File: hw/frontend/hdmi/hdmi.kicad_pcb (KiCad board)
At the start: 6 copper layers, 100 x 100 mm, 208 parts, among them J801 SAMTEC_QSH-090-D, P201 HDMI, P301 HDMI, P302 CONN_02X05, P601 CONN_02X03, P602 CONN_02X05, P801 CONN_01X02, U202 TPD12S520, U301 TPD12S521, U302 PTN3360DBS, U401 TLK3134-MULTI, U701 SI5338B, U801 ON_CAT24C256, U901 TPS54218, U902 TPS54218, U903 MIC5207-2.5YM5, U904 TPS54218, U905 FAN4860UMP

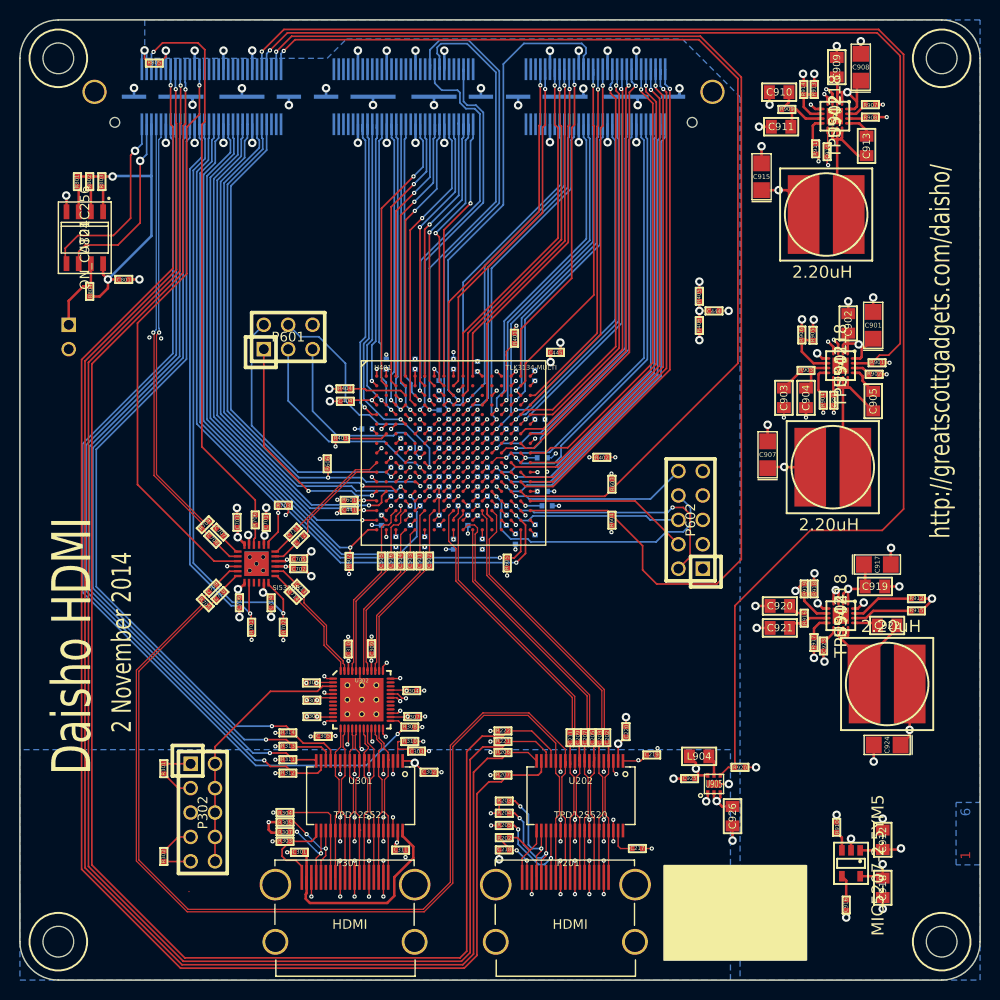
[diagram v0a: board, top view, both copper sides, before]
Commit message: hdmi: fixed some bad footprints
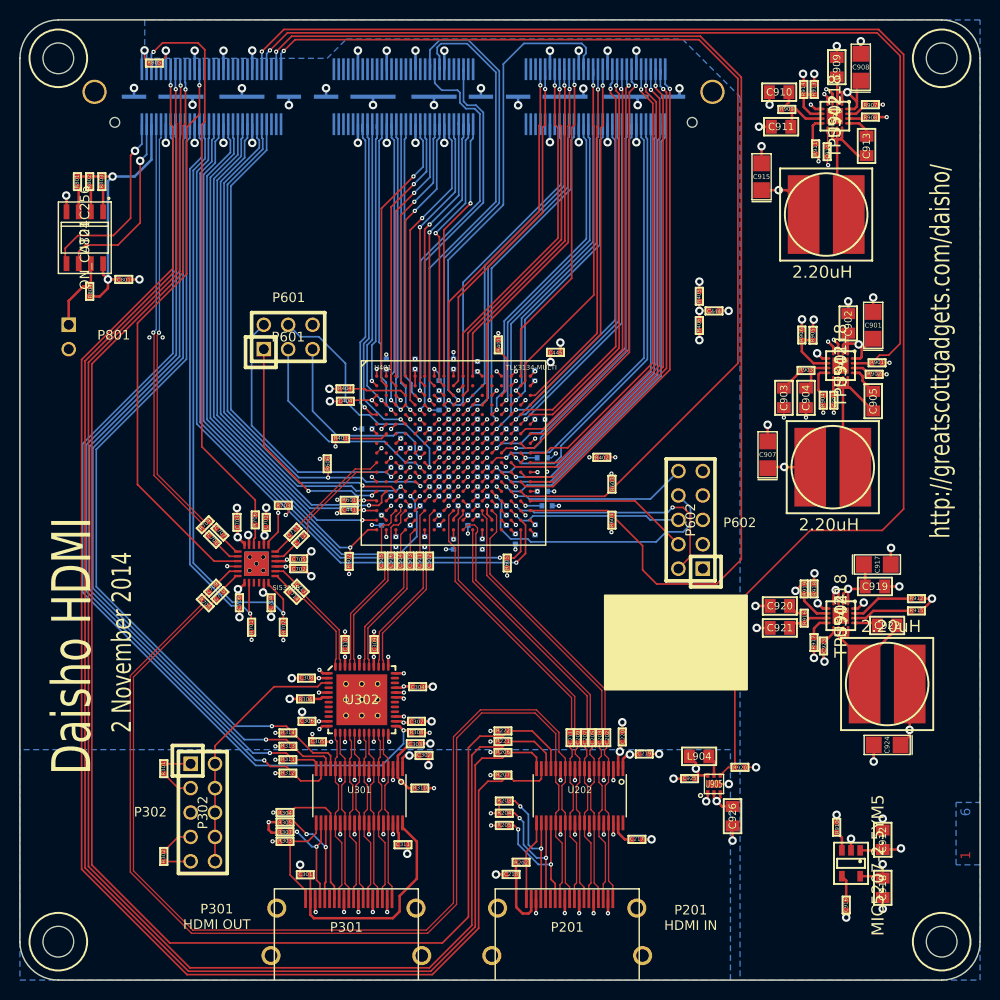
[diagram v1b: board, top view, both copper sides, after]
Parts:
- P201, P301: footprint daisho:GSG-MOLEX-HDMI -> daisho:10029449-111RLF
- U302: footprint daisho:GSG-QFN48-6 -> daisho:QFN48-7
- moved P201 10.7 mm to (257.0, 200.0)
- moved P301 10.7 mm to (234.0, 200.0)
- moved R310 4.97 mm to (241.7, 180.0)
- moved R202 3.11 mm to (252.2, 187.7)
- moved C218 2.66 mm to (251.2, 189.0)
- moved C301 2.42 mm to (229.7, 189.0)
- moved C302 1.82 mm to (242.1, 176.6)
- moved R401 1.82 mm to (249.8, 133.8)
- moved C217 0.96 mm to (264.3, 185.3)
- moved R308 0.91 mm to (241.3, 174.2)
- moved C305 0.82 mm to (231.0, 175.2)
- moved C219 0.79 mm to (265.0, 176.5)
- moved C303 0.78 mm to (241.2, 175.4)
- moved C304 0.74 mm to (241.4, 169.4)
- moved C306 0.71 mm to (229.9, 173.1)
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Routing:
- net GND: track 264.3 -> 235.1 mm, vias 244 -> 228
- net CLK_IN_P_SUPP: track 110.5 -> 118.2 mm
- net CLK_IN_M_SUPP: track 110.8 -> 118.1 mm
- net Net-(P301-Pad13): track 10.8 -> 14.2 mm
- net V1P2_REGULATED: track 43.1 -> 40.1 mm
- net Net-(P201-Pad13): track 12.1 -> 15.0 mm
- net Net-(P301-Pad15): track 9.94 -> 12.8 mm
- net Net-(P201-Pad16): track 12.6 -> 15.2 mm
- net /Mezzanine/FE_I2C_VCC: track 33.1 -> 30.5 mm
- net Net-(P301-Pad16): track 9.23 -> 11.7 mm
- net Net-(P201-Pad15): track 12.7 -> 15.1 mm
- net Net-(C303-Pad1): track 4.21 -> 6.57 mm
- net /HDMI Output/HDMI_OUT_D2_P_SHIFTED: track 17.5 -> 19.7 mm
- net CEC_IN_SUPP: track 162.7 -> 160.5 mm
- net Net-(C218-Pad1): track 6.25 -> 8.15 mm, vias 2 -> 0
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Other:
- board text added: "P201 HDMI IN"
- board text added: "P301 HDMI OUT"
- board text added: "P302"
- board text added: "P601"
- board text added: "P602"
- board text added: "P801"

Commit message: hdmi: renamed layers
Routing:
- added copper zone on C4.Cu, net /Serdes Power/VREF
- added copper zone on C2.Cu, net GND
- added copper zone on C5.Cu, net GND
- added copper zone on C4.Cu, net V1P2_REGULATED
- added copper zone on C3.Cu, net V1P5_REGULATED
- added copper zone on C3.Cu, net V2P5_REGULATED
- added copper zone on C4.Cu, net V3P3_REGULATED
- removed copper zone on Inner2.Cu, net /Serdes Power/VREF
- removed copper zone on Inner1.Cu, net GND
- removed copper zone on Inner4.Cu, net GND
- removed copper zone on Inner2.Cu, net V1P2_REGULATED
- removed copper zone on Inner3.Cu, net V1P5_REGULATED
- removed copper zone on Inner3.Cu, net V2P5_REGULATED
- removed copper zone on Inner2.Cu, net V3P3_REGULATED

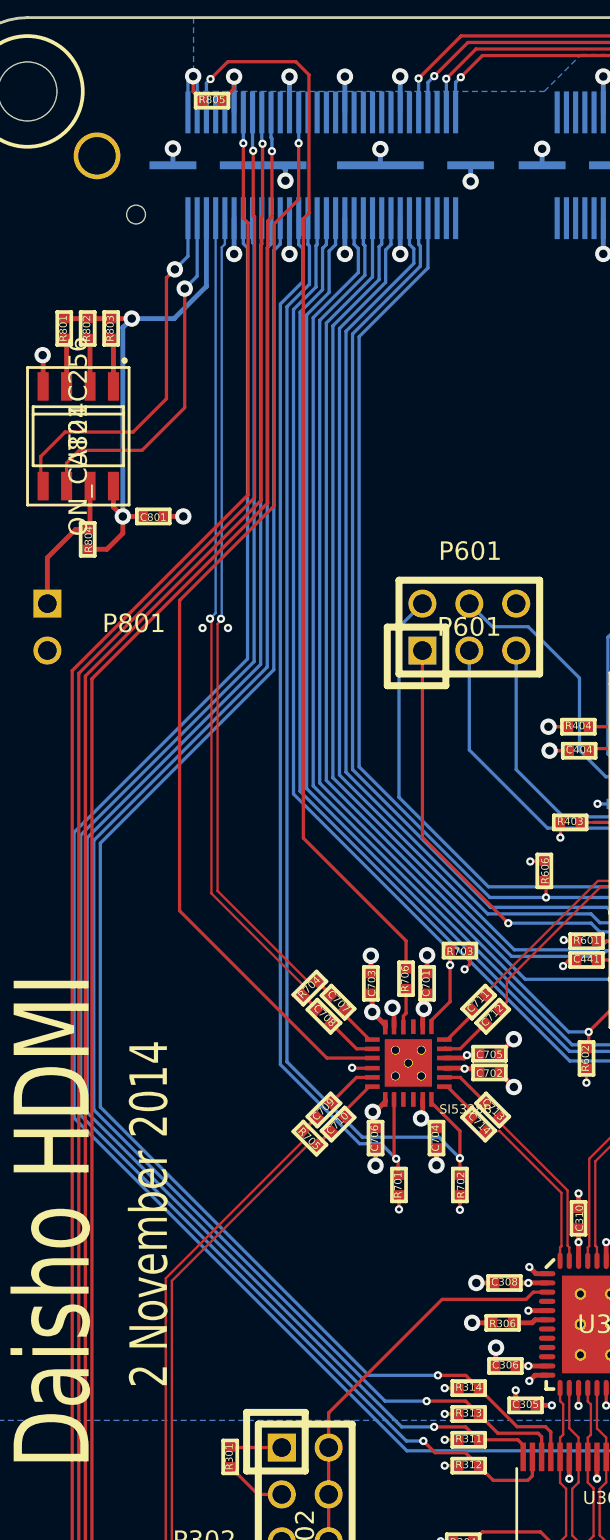
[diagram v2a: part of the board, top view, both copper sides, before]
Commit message: hdmi: fixed up Si5338 footprint
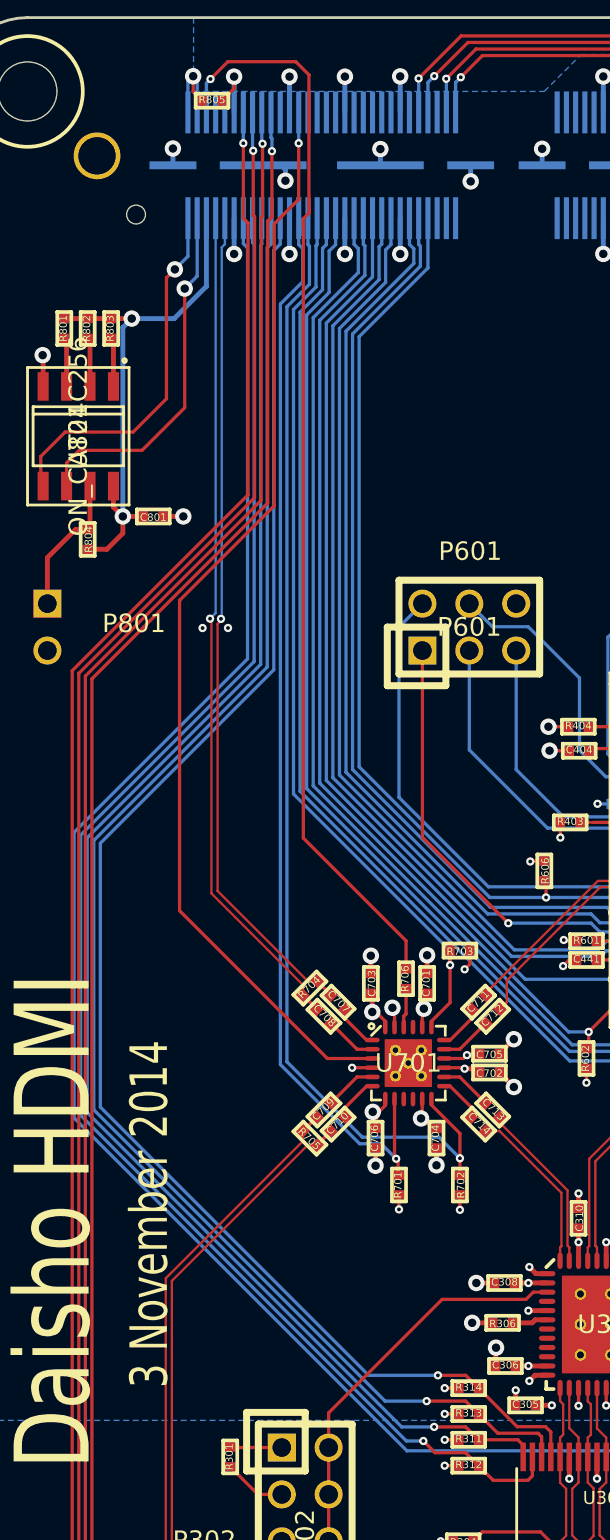
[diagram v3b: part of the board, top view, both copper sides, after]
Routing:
- net V2P5_REGULATED: track 63.5 -> 64.2 mm
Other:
- board text added: "3 November 2014"
- board text removed: "2 November 2014"

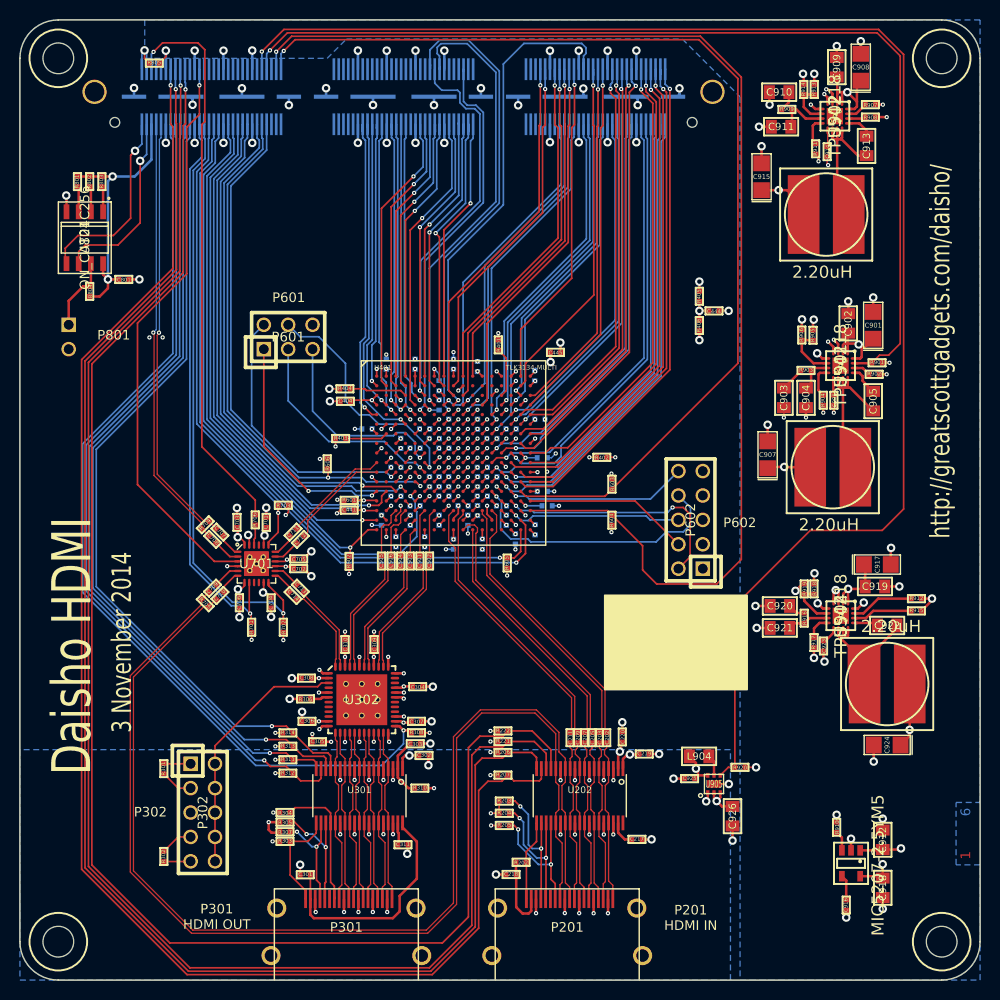
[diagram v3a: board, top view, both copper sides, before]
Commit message: hdmi: bottom heat sinks under QFNs
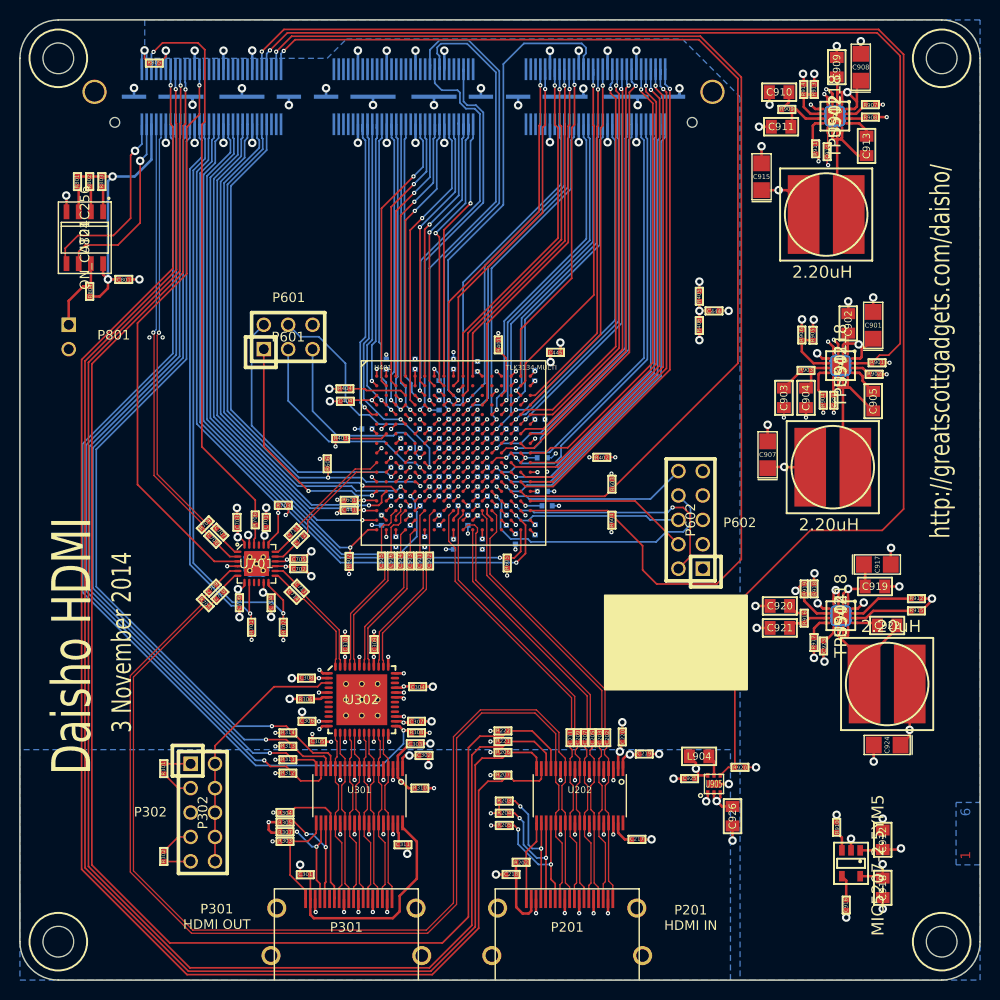
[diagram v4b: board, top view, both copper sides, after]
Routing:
- net GND: track 235.3 -> 285.2 mm
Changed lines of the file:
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@@
     (thickness 1.6)
     (drawings 23)
-    (tracks 3885)
+    (tracks 3919)
     (zones 0)
     (modules 208)
@@
   )
   (setup
-    (last_trace_width 0.1778)
+    (last_trace_width 1.27)
     (user_trace_width 0.127)
     (user_trace_width 0.26416)
@@
     (aux_axis_origin 0 0)
     (grid_origin 200 100)
-    (visible_elements FFFEFFFF)
+    (visible_elements FFFCFFFF)
     (pcbplotparams
       (layerselection 0x010fc_8000001f)
@@
   (segment (start 261.306984 182.630284) (end 261.306984 183.626118) (width 0.127) (layer C1F.Cu) (net 19))
   (segment (start 261.306984 177.976118) (end 261.306984 179.391236) (width 0.127) (layer C1F.Cu) (net 19))
-  (segment (start 223.888 154.692) (end 223.888 153.7584) (width 0.1778) (layer C1F.Cu) (net 20) (status 400000))
+  (segment (start 284.375404 110.524298) (end 284.375404 109.523538) (width 1.27) (layer C6B.Cu) (net 20))
+  (segment (start 284.375404 109.523538) (end 285.376164 109.523538) (width 1.27) (layer C6B.Cu) (net 20))
+  (segment (start 285.376164 109.523538) (end 285.376164 110.524298) (width 1.27) (layer C6B.Cu) (net 20))
+  (segment (start 285.376164 110.524298) (end 284.375404 110.524298) (width 1.27) (layer C6B.Cu) (net 20))
+  (segment (start 284.968604 135.506738) (end 285.969364 135.506738) (width 1.27) (layer C6B.Cu) (net 20))
+  (segment (start 285.969364 135.506738) (end 285.969364 136.507498) (width 1.27) (layer C6B.Cu) (net 20))
+  (segment (start 285.969364 136.507498) (end 284.968604 136.507498) (width 1.27) (layer C6B.Cu) (net 20))
+  (segment (start 284.968604 136.507498) (end 284.968604 135.506738) (width 1.27) (layer C6B.Cu) (net 20))
+  (segment (start 284.968604 135.506738) (end 285.036738 135.506738) (width 1.27) (layer C6B.Cu) (net 20))
+  (segment (start 285.036738 135.506738) (end 285.09 135.56) (width 1.27) (layer C6B.Cu) (net 20))
+  (segment (start 285.09 135.56) (end 284.968604 135.506738) (width 1.27) (layer C6B.Cu) (net 20))
+  (segment (start 284.99562 161.55162) (end 285.99638 161.55162) (width 1.27) (layer C6B.Cu) (net 20))
+  (segment (start 285.99638 161.55162) (end 285.99638 162.55238) (width 1.27) (layer C6B.Cu) (net 20))
+  (segment (start 285.99638 162.55238) (end 284.99562 162.55238) (width 1.27) (layer C6B.Cu) (net 20))
+  (segment (start 284.99562 162.55238) (end 284.99562 161.55162) (width 1.27) (layer C6B.Cu) (net 20))
+  (segment (start 233.956984 169.151118) (end 233.956984 172.451118) (width 1.27) (layer C6B.Cu) (net 20))
+  (segment (start 233.956984 172.451118) (end 235.606984 172.451118) (width 1.27) (layer C6B.Cu) (net 20))
+  (segment (start 235.606984 172.451118) (end 237.256984 170.801118) (width 1.27) (layer C6B.Cu) (net 20))
+  (segment (start 237.256984 170.801118) (end 237.256984 170.820016) (width 1.27) (layer C6B.Cu) (net 20))
+  (segment (start 237.256984 170.820016) (end 237.1348 170.9422) (width 1.27) (layer C6B.Cu) (net 20))
+  (segment (start 237.1348 170.9422) (end 237.256984 170.801118) (width 1.27) (layer C6B.Cu) (net 20))
+  (segment (start 237.256984 172.451118) (end 233.956984 169.151118) (width 1.27) (layer C6B.Cu) (net 20))
+  (segment (start 233.956984 169.151118) (end 237.256984 169.151118) (width 1.27) (layer C6B.Cu) (net 20))
+  (segment (start 237.256984 169.151118) (end 233.956984 172.451118) (width 1.27) (layer C6B.Cu) (net 20))
+  (segment (start 233.956984 172.451118) (end 237.256984 172.451118) (width 1.27) (layer C6B.Cu) (net 20))
+  (segment (start 237.256984 172.451118) (end 237.256984 169.151118) (width 1.27) (layer C6B.Cu) (net 20))
+  (segment (start 237.256984 169.151118) (end 235.606984 169.151118) (width 1.27) (layer C6B.Cu) (net 20))
+  (segment (start 235.606984 169.151118) (end 233.956984 170.801118) (width 1.27) (layer C6B.Cu) (net 20))
+  (segment (start 233.956984 170.801118) (end 233.956984 170.919616) (width 1.27) (layer C6B.Cu) (net 20))
+  (segment (start 223.938 155.942) (end 225.338 155.942) (width 1.27) (layer C6B.Cu) (net 20))
+  (segment (start 225.338 155.942) (end 225.338 157.342) (width 1.27) (layer C6B.Cu) (net 20))
+  (segment (start 225.338 157.342) (end 223.938 157.342) (width 1.27) (layer C6B.Cu) (net 20))
+  (segment (start 223.938 157.342) (end 223.938 155.942) (width 1.27) (layer C6B.Cu) (net 20))
+  (segment (start 223.938 155.942) (end 224.638 156.642) (width 1.27) (layer C6B.Cu) (net 20))
+  (segment (start 223.888 154.692) (end 223.888 153.7584) (width 0.1778) (layer C1F.Cu) (net 20))
   (via (at 223.7744 153.6448) (size 0.889) (drill 0.4572) (layers C1F.Cu C6B.Cu) (net 20))
   (segment (start 223.7744 153.6448) (end 223.863 153.7334) (width 0.26416) (layer C1F.Cu) (net 20))
@@
   (segment (start 211.3534 127.0254) (end 212.4456 127.0254) (width 0.26416) (layer C1F.Cu) (net 20))
   (via (at 212.4456 127.0254) (size 0.889) (drill 0.4572) (layers C1F.Cu C6B.Cu) (net 20))
-  (segment (start 272.288 179.578) (end 273.82978 179.578) (width 0.1778) (layer C1F.Cu) (net 20))
+  (segment (start 272.288 179.578) (end 273.82978 179.578) (width 0.26416) (layer C1F.Cu) (net 20))
   (via (at 273.83232 179.58054) (size 0.889) (drill 0.4572) (layers C1F.Cu C6B.Cu) (net 20))
   (segment (start 273.82978 179.578) (end 273.83232 179.58054) (width 0.1778) (layer C1F.Cu) (net 20))
@@
   (segment (start 286.944724 135.758198) (end 288.684504 135.758198) (width 0.26416) (layer C1F.Cu) (net 167))
   (segment (start 288.684504 135.758198) (end 288.735584 135.707118) (width 0.26416) (layer C1F.Cu) (net 167))
+  (segment (start 236.656984 147.601118) (end 238.656984 145.601118) (width 0.1778) (layer C3.Cu) (net 168))
   (via (at 251.606984 153.551118) (size 0.44958) (layers C1F.Cu C6B.Cu) (net 168))
   (segment (start 251.606984 153.551118) (end 251.156984 153.101118) (width 0.1778) (layer C1F.Cu) (net 168))
@@
   (via (at 238.656984 145.601118) (size 0.44958) (layers C1F.Cu C6B.Cu) (net 168))
   (segment (start 238.656984 145.601118) (end 238.156984 146.101118) (width 0.1778) (layer C1F.Cu) (net 168))
-  (segment (start 236.656984 147.601118) (end 238.656984 145.601118) (width 0.1778) (layer C3.Cu) (net 168))
   (segment (start 236.656984 139.601118) (end 234.545962 139.601118) (width 0.1778) (layer C1F.Cu) (net 169))
   (segment (start 234.545962 139.601118) (end 234.42676 139.72032) (width 0.1778) (layer C1F.Cu) (net 169))
@@
   (via (at 281.559 105.6132) (size 0.889) (drill 0.4572) (layers C1F.Cu C6B.Cu) (net 169))
   (segment (start 281.6352 106.7054) (end 281.6352 105.6894) (width 0.26416) (layer C1F.Cu) (net 169))
-  (segment (start 223.388 154.692) (end 223.388 154.376) (width 0.1778) (layer C1F.Cu) (net 170) (status C00000))
-  (segment (start 223.388 154.376) (end 222.8854 153.8734) (width 0.1778) (layer C1F.Cu) (net 170) (status 400000))
+  (segment (start 223.388 154.692) (end 223.388 154.376) (width 0.1778) (layer C1F.Cu) (net 170))
+  (segment (start 223.388 154.376) (end 222.8854 153.8734) (width 0.1778) (layer C1F.Cu) (net 170))
   (segment (start 222.8854 153.8734) (end 222.6822 153.8734) (width 0.1778) (layer C1F.Cu) (net 170))
   (segment (start 222.6822 153.8734) (end 222.7076 153.8988) (width 0.1778) (layer C1F.Cu) (net 170))
@@
   (segment (start 205.08 129.2608) (end 205.08 131.75) (width 0.26416) (layer C1F.Cu) (net 196))
   (segment (start 207.264 127.7366) (end 206.6042 127.7366) (width 0.26416) (layer C1F.Cu) (net 196))
-  (segment (start 224.388 154.692) (end 224.388 154.098) (width 0.1778) (layer C1F.Cu) (net 197) (status 400000))
-  (segment (start 224.511 153.975) (end 224.511 152.6034) (width 0.1778) (layer C1F.Cu) (net 197) (status 800000))
+  (segment (start 224.388 154.692) (end 224.388 154.098) (width 0.1778) (layer C1F.Cu) (net 197))
+  (segment (start 224.511 153.975) (end 224.511 152.6034) (width 0.1778) (layer C1F.Cu) (net 197))
   (segment (start 224.388 154.098) (end 224.511 153.975) (width 0.1778) (layer C1F.Cu) (net 197))
   (segment (start 206.121 119.982) (end 206.121 117.5004) (width 0.26416) (layer C1F.Cu) (net 198))
